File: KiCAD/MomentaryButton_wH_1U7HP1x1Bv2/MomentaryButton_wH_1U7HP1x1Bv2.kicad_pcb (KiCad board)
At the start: 2 copper layers, 35.2 x 39.7 mm, 4 parts, among them SW1 SW_SPST_M16_Panel_Mount_Push-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

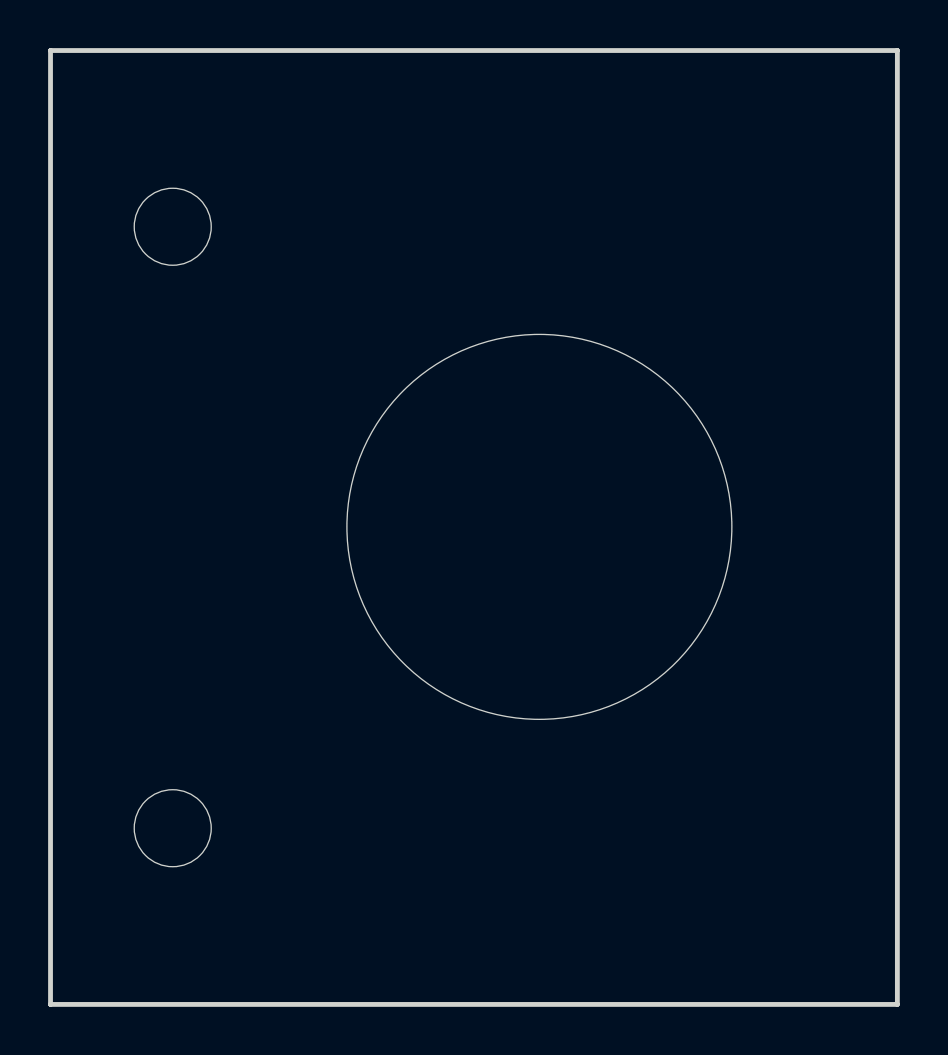
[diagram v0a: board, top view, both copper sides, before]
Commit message: updated all modules to use plated through-holes wherever possible
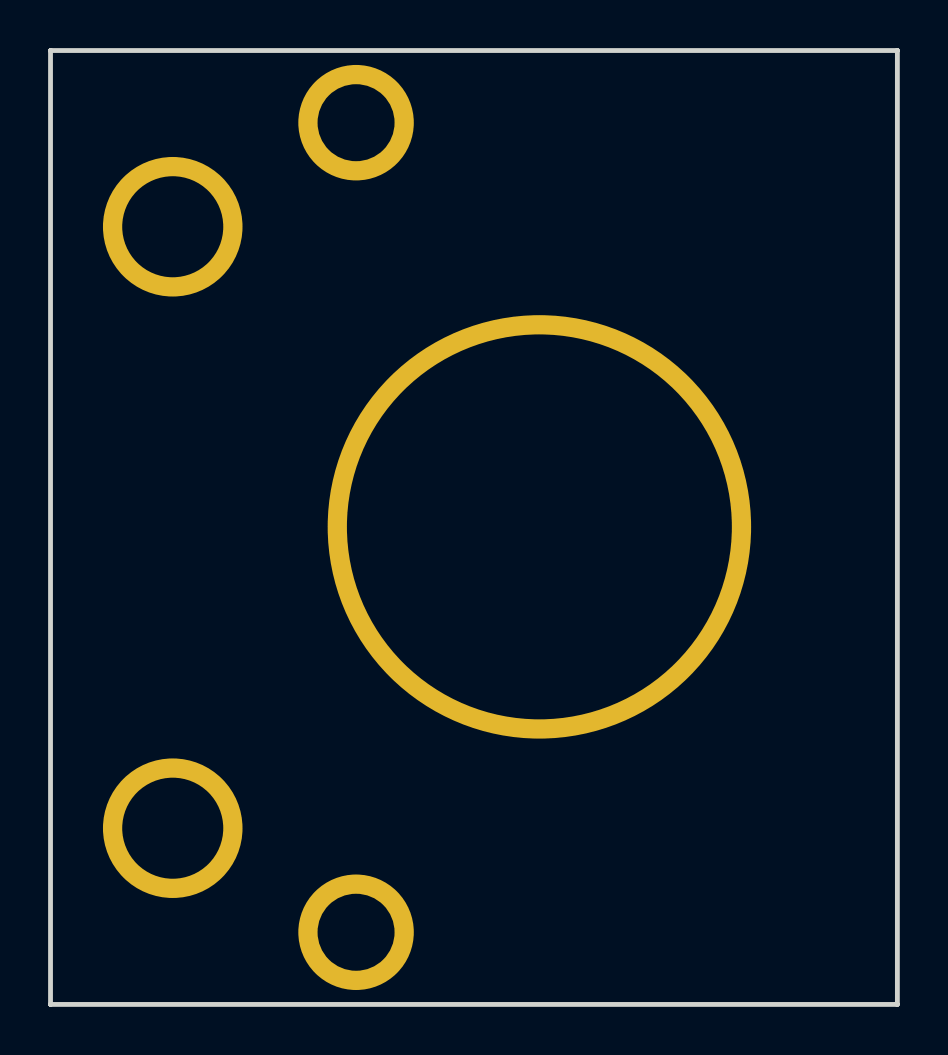
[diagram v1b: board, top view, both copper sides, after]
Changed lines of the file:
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@@
+			)
+		)
+		(property "Source" "https://www.aliexpress.com/item/1005007242440186.html"
+			(at 0 36 0)
+			(layer "F.Fab")
+			(hide yes)
+			(effects
+				(font
+					(size 1 1)
+					(thickness 0.1)
+				)
 			)
 		)
@@
 			)
 		)
-		(pad "" np_thru_hole circle
+		(pad "" thru_hole circle
 			(at 0 0)
-			(size 3.2 3.2)
-			(drill 3.2)
-			(layers "*.Cu" "*.Mask")
-		)
-		(pad "" np_thru_hole circle
+			(size 5.8 5.8)
+			(drill 4.2)
+			(layers "*.Cu" "*.Mask")
+			(remove_unused_layers no)
+		)
+		(pad "" thru_hole circle
 			(at 0 25)
-			(size 3.2 3.2)
-			(drill 3.2)
-			(layers "*.Cu" "*.Mask")
+			(size 5.8 5.8)
+			(drill 4.2)
+			(layers "*.Cu" "*.Mask")
+			(remove_unused_layers no)
 		)
 		(embedded_fonts no)
@@
 			)
 		)
-		(pad "" np_thru_hole oval
+		(pad "" thru_hole circle
 			(at 0 0)
-			(size 4.34 3.2)
-			(drill oval 4.34 3.2)
-			(layers "*.Cu" "*.Mask")
+			(size 4.8 4.8)
+			(drill 3.2)
+			(layers "*.Cu" "*.Mask")
+			(remove_unused_layers no)
 		)
 		(embedded_fonts no)
@@
 			)
 		)
-		(pad "" np_thru_hole oval
+		(pad "" thru_hole circle
 			(at 0 0)
-			(size 4.34 3.2)
-			(drill oval 4.34 3.2)
-			(layers "*.Cu" "*.Mask")
+			(size 4.8 4.8)
+			(drill 3.2)
+			(layers "*.Cu" "*.Mask")
+			(remove_unused_layers no)
 		)
 		(embedded_fonts no)
@@
 			)
 		)
-		(pad "" np_thru_hole circle
+		(pad "" thru_hole circle
 			(at 0 0)
-			(size 16 16)
+			(size 17.6 17.6)
 			(drill 16)
 			(layers "*.Cu" "*.Mask")
+			(remove_unused_layers no)
 		)
 		(embedded_fonts no)
